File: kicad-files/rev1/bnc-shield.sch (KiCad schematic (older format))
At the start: 113 parts

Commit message: improve robustness and leakage for bnc shield
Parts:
- removed C? (x15): 100nF, symbol C
- removed P? (x7): BNC, symbol BNC
- removed R? (x8): 100k, symbol R
- removed R? (x7): 1.5k, symbol R
- removed R? (x7): 10k, symbol R
- removed U? (x16): SN74LVC1G3157, symbol SN74LVC1G3157
- added C? (x15): 100nF, symbol C
- added P? (x7): BNC, symbol BNC
- added R? (x8): 1M, symbol R
- added R? (x7): 1.5k, symbol R
- added R? (x7): 10k, symbol R
- added U? (x16): TS5A4624, symbol TS5A4624
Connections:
- net labels removed: +5V
- wire segments 432 -> 440
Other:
- moved on the sheet: C?, R?

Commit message: fixed 2.5V regulator resistors
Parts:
- R?: value 124k -> 43.2k
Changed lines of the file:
@@
-EESchema Schematic File Version 2  date Mon 27 May 2013 04:02:44 AM UTC
+EESchema Schematic File Version 2  date Mon 27 May 2013 01:39:56 PM UTC
 LIBS:power
 LIBS:device
@@
 P 6150 8950
 F 0 "R?" V 6230 8950 50  0000 C CNN
-F 1 "124k" V 6150 8950 50  0000 C CNN
+F 1 "43.2k" V 6150 8950 50  0000 C CNN
 F 2 "SM0603" H 6150 8950 60  0001 C CNN
 	1    6150 8950

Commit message: add RS-485 and headers to bnc-shield
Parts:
- removed L?: INDUCTOR, symbol INDUCTOR
- removed P?: CONN_4X2, symbol CONN_4X2
- added C? (x4): 100nF, symbol C
- added C?: 10uF, symbol C
- added D? (x4): DOUBLE_SCHOTTKY, symbol DOUBLE_SCHOTTKY
- added J? (x2): RJ45, symbol RJ45
- added L? (x2): INDUCTOR, symbol INDUCTOR
- added P?: CONN_8X2, symbol CONN_8X2
- added P?: CONN_4, symbol CONN_4
- added P?: ARDUINO_SHIELD, symbol ARDUINO_SHIELD
- added R? (x6): 1k, symbol R
- added R? (x3): 100k, symbol R
- added R?: 120, symbol R
- added R? (x2): 680, symbol R
- added U?: RS485, symbol RS485
- added U? (x2): TS5A4624, symbol TS5A4624
- added U?: 74HC00, symbol 7400
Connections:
- net labels added: +5V, 5V_IN, ADS129x_GPIO1, ADS129x_GPIO2, ADS129x_GPIO3, ADS129x_GPIO4, DAISY_DETECT_NEXT, DAISY_DETECT_NEXT_FILT, DAISY_DETECT_PREVIOUS, DAISY_DETECT_PREVIOUS_FILT, DAISY_ENUMERATION_IN, DAISY_ENUMERATION_IN_FILT, DAISY_ENUMERATION_OUT, DAISY_ENUMERATION_OUT_FILT, GND, PA16, PA17, PA18, PA22, PA23, PA24, PA25, PA26, PA27, PA28, PA29, PA4, PA6, PA8, PA9, PB25, PB27, PC21, PC22, PC23, PC24, PC25, PC26, PC28, PC29, PD7, PD8, RESET, RS485_A, RS485_B, RTS2_RS485_DE, RXD2_RS485_R, TXD2_RS485_D, V_IN
- wire segments 440 -> 606
- no-connect marks 16 -> 19
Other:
- note added: "Biasing and termination for RS-485"
- note added: "DAISY CHAIN NEXT"
- note added: "DAISY CHAIN PREVIOUS"
- note added: "TODO: Replace with SN74LVC1G00DCKR"
- note added: "TODO: according to the SN65HVD78D datasheet, \n we may not need the biasing resistors \n (allowing us to eleminate a switch). \n We should discuss this."
- note added: "e.g. SN65HVD78D"

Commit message: improve text label names
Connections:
- net labels added: PA16_A0, PA17_SDA1, PA18_SCL1, PA22_A3, PA23_A2, PA24_A1, PA25_MISO, PA26_MOSI, PA27_SCLK, PA28_SS0, PA29_SS1, PA4_A5, PA6_A4, PA8_RX, PA9_TX, PB25_PWM2, PB27_PWM13, PC21_PWM9, PC22_PWM8, PC23_PWM7, PC24_PWM6, PC25_PWM5, PC26_PWM4, PC28_PWM3, PC29_PWM10, PD7_PWM11, PD8_PWM12
- net labels removed: PA16, PA17, PA18, PA22, PA23, PA24, PA25, PA26, PA27, PA28, PA29, PA4, PA6, PA8, PA9, PB25, PB27, PC21, PC22, PC23, PC24, PC25, PC26, PC28, PC29, PD7, PD8
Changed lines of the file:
@@
 RESET
 Text Label 26000 5300 0    60   ~ 0
-PA27
+PA27_SCLK
 Text Label 26000 5200 0    60   ~ 0
-PA25
+PA25_MISO
 Text Label 29000 5300 2    60   ~ 0
-PA26
+PA26_MOSI
 $Comp
 L GND #PWR?
@@
 NoConn ~ 29600 3050
 Text Label 29600 2850 2    60   ~ 0
-PA18
+PA18_SCL1
 Text Label 29600 2950 2    60   ~ 0
-PA17
+PA17_SDA1
 $Comp
 L GND #PWR?
@@
 $EndComp
 Text Label 29600 3250 2    60   ~ 0
-PB27
+PB27_PWM13
 Text Label 29600 3350 2    60   ~ 0
-PD8
+PD8_PWM12
 Text Label 29600 3450 2    60   ~ 0
-PD7
+PD7_PWM11
 Text Label 30100 3450 2    60   ~ 0
-PC29
+PC29_PWM10
 Text Label 30100 3550 2    60   ~ 0
-PA28
+PA28_SS0
 Text Label 29600 3650 2    60   ~ 0
-PC21
+PC21_PWM9
 Text Label 29600 3750 2    60   ~ 0
-PC22
+PC22_PWM8
 Text Label 29600 3950 2    60   ~ 0
-PC23
+PC23_PWM7
 Text Label 29600 4050 2    60   ~ 0
-PC24
+PC24_PWM6
 Text Label 29600 4150 2    60   ~ 0
-PC25
+PC25_PWM5
 Text Label 30100 4150 2    60   ~ 0
-PC26
+PC26_PWM4
 Text Label 30100 4250 2    60   ~ 0
-PA29
+PA29_SS1
 Text Label 29600 4350 2    60   ~ 0
-PC28
+PC28_PWM3
 Text Label 29600 4450 2    60   ~ 0
-PB25
+PB25_PWM2
 Text Label 29600 4550 2    60   ~ 0
-PA9
+PA9_TX
 Text Label 29600 4650 2    60   ~ 0
-PA8
+PA8_RX
 Text Label 25500 4650 0    60   ~ 0
-PA4
+PA4_A5
 Text Label 25500 4550 0    60   ~ 0
-PA6
+PA6_A4
 Text Label 25500 4450 0    60   ~ 0
-PA22
+PA22_A3
 Text Label 25500 4350 0    60   ~ 0
-PA23
+PA23_A2
 Text Label 25500 4250 0    60   ~ 0
-PA24
+PA24_A1
 Text Label 25500 4150 0    60   ~ 0
-PA16
+PA16_A0
 $Comp
 L GND #PWR?

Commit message: tidy up the labels and wires on the shields
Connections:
- wire segments 606 -> 744

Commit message: added isolation to BNC shield
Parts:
- removed C? (x2): 10uF, symbol C
- removed C? (x2): 100nF, symbol C
- removed R? (x2): 100k, symbol R
- added C? (x4): 10uF, symbol C
- added C? (x4): 100nF, symbol C
- added L? (x4): MH2029-221Y, symbol INDUCTOR
- added R? (x2): 100k, symbol R
- added U?: SI8661, symbol SI8661
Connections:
- net labels added: LED_LATCH_CLK_ISO, LED_OUTPUT_ENABLE_INPUT_ISO, LED_SERIAL_DAISY_2, LED_SERIAL_DAISY_2_ISO, LED_SERIAL_DAISY_4, LED_SERIAL_DAISY_4_ISO, LED_SHIFT_REG_CLEAR_ISO, LED_SHIFT_REG_CLK_ISO
- wire segments 744 -> 657
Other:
- note added: "Isolated"
- note added: "Not isolated"
- moved on the sheet: C?, D?, L?, P?, R?, U?

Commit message: remove RS-485
 The purpose of the RS-485 was to allow us to synch multiple
devices. However, a better way to do this is to inject a counter
into the samples using the USB Start Of Frame which will be
shared by all devices on the same USB bus.
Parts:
- removed C? (x4): 100nF, symbol C
- removed C?: 10uF, symbol C
- removed D? (x4): DOUBLE_SCHOTTKY, symbol DOUBLE_SCHOTTKY
- removed J? (x2): RJ45, symbol RJ45
- removed L?: INDUCTOR, symbol INDUCTOR
- removed P?: CONN_8X2, symbol CONN_8X2
- removed R? (x6): 1k, symbol R
- removed R? (x3): 100k, symbol R
- removed R?: 120, symbol R
- removed R? (x2): 680, symbol R
- removed U?: RS485, symbol RS485
- removed U? (x2): TS5A4624, symbol TS5A4624
- removed U?: 74HC00, symbol 7400
- added P12: CONN_4X2, symbol CONN_4X2
- gave numbers to parts that had none: 123
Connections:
- net labels removed: 5V_IN, DAISY_DETECT_NEXT, DAISY_DETECT_NEXT_FILT, DAISY_DETECT_PREVIOUS, DAISY_DETECT_PREVIOUS_FILT, DAISY_ENUMERATION_IN, DAISY_ENUMERATION_IN_FILT, DAISY_ENUMERATION_OUT, DAISY_ENUMERATION_OUT_FILT, RS485_A, RS485_B, RTS2_RS485_DE, RXD2_RS485_R, TXD2_RS485_D
- wire segments 657 -> 537
- no-connect marks 19 -> 17
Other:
- note removed: "Biasing and termination for RS-485"
- note removed: "DAISY CHAIN NEXT"
- note removed: "DAISY CHAIN PREVIOUS"
- note removed: "TODO: Replace with SN74LVC1G00DCKR"
- note removed: "TODO: according to the SN65HVD78D datasheet, \n we may not need the biasing resistors \n (allowing us to eleminate a switch). \n We should discuss this."
- note removed: "e.g. SN65HVD78D"

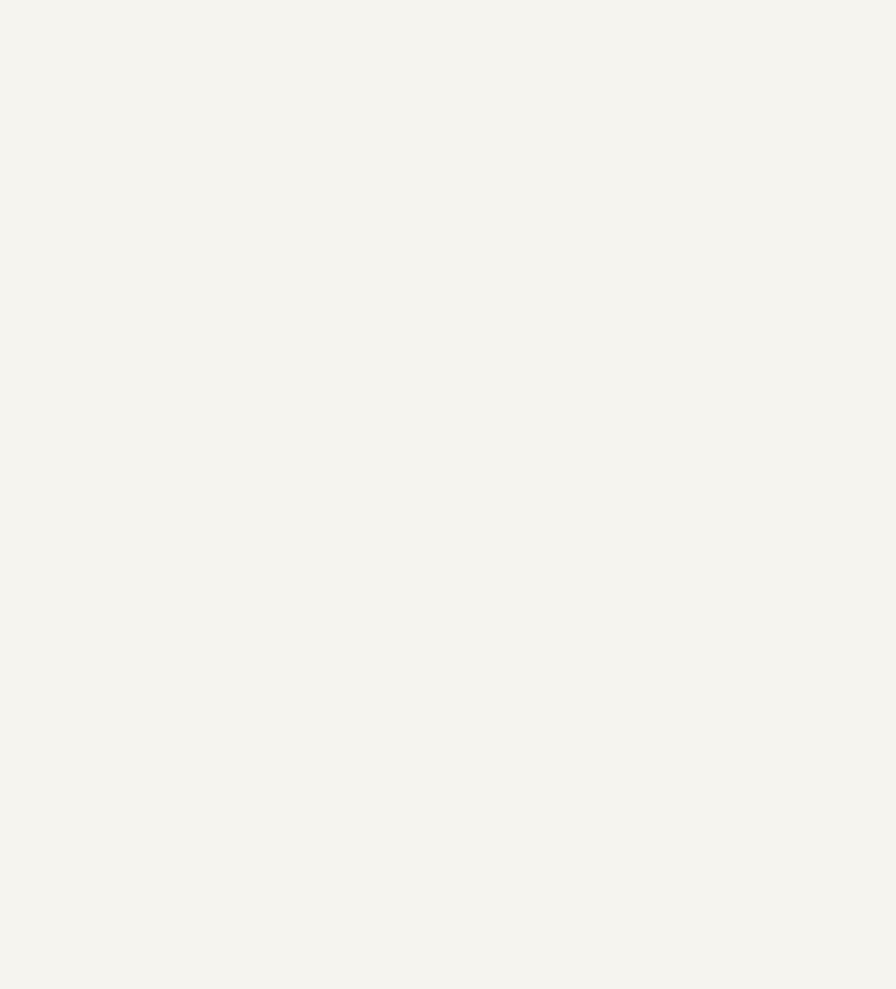
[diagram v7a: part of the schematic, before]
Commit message: added I2C EEPROM to shields
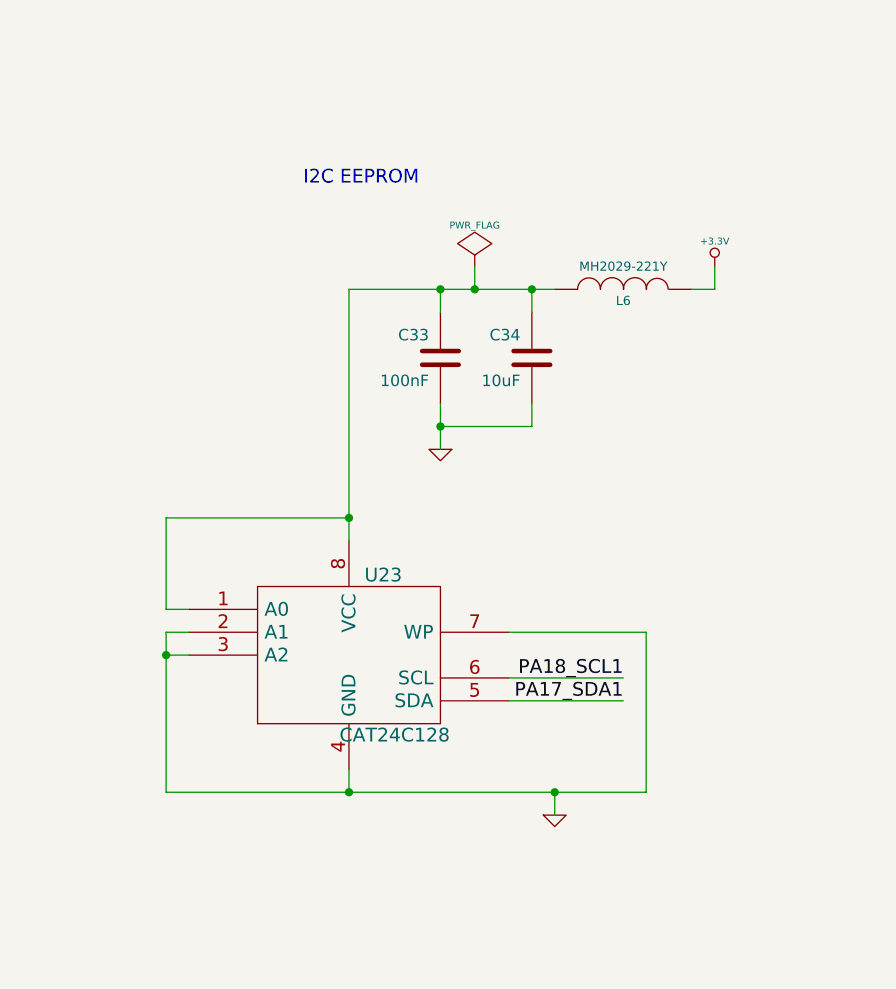
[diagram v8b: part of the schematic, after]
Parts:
- added C33: 100nF, symbol C
- added C34: 10uF, symbol C
- added L6: MH2029-221Y, symbol INDUCTOR
- added U23: CAT24C128, symbol 24C16
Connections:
- wire segments 537 -> 560
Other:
- note added: "I2C EEPROM"
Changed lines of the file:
@@
-EESchema Schematic File Version 2  date Sat 22 Jun 2013 01:22:06 PM CEST
+EESchema Schematic File Version 2  date Sat 22 Jun 2013 02:00:34 PM CEST
 LIBS:power
 LIBS:device
@@
 Comment4 ""
 $EndDescr
+Text Notes 18000 11500 0    60   ~ 0
+I2C EEPROM
+Text Label 19400 13750 2    60   ~ 0
+PA17_SDA1
+Text Label 19400 13650 2    60   ~ 0
+PA18_SCL1
+$Comp
+L GND #PWR79
+U 1 1 51C590FD
+P 19100 14250
+F 0 "#PWR79" H 19100 14250 30  0001 C CNN
+F 1 "GND" H 19100 14180 30  0001 C CNN
+	1    19100 14250
+	1    0    0    -1
+$EndComp
+$Comp
+L GND #PWR76
+U 1 1 51C590FC
+P 18600 12650
+F 0 "#PWR76" H 18600 12650 30  0001 C CNN
+F 1 "GND" H 18600 12580 30  0001 C CNN
+	1    18600 12650
+	-1   0    0    -1
+$EndComp
+$Comp
+L +3.3V #PWR80
+U 1 1 51C590FB
+P 19800 11850
+F 0 "#PWR80" H 19800 11810 30  0001 C CNN
+F 1 "+3.3V" H 19800 11960 30  0000 C CNN
+	1    19800 11850
+	-1   0    0    -1
+$EndComp
+$Comp
+L C C33
+U 1 1 51C590FA
+P 18600 12250
+F 0 "C33" H 18650 12350 50  0000 L CNN
+F 1 "100nF" H 18650 12150 50  0000 L CNN
+	1    18600 12250
+	-1   0    0    -1
+$EndComp
+$Comp
+L INDUCTOR L6
+U 1 1 51C590F9
+P 19400 11950
+F 0 "L6" V 19350 11950 40  0000 C CNN
+F 1 "MH2029-221Y" V 19500 11950 40  0000 C CNN
+	1    19400 11950
+	0    1    -1   0
+$EndComp
+$Comp
+L C C34
+U 1 1 51C590F8
+P 19000 12250
+F 0 "C34" H 19050 12350 50  0000 L CNN
+F 1 "10uF" H 19050 12150 50  0000 L CNN
+	1    19000 12250
+	-1   0    0    -1
+$EndComp
+$Comp
+L PWR_FLAG #FLG8
+U 1 1 51C590F7
+P 18750 11850
+F 0 "#FLG8" H 18750 11945 30  0001 C CNN
+F 1 "PWR_FLAG" H 18750 12030 30  0000 C CNN
+	1    18750 11850
+	-1   0    0    -1
+$EndComp
+$Comp
+L 24C16 U23
+U 1 1 51C590F6
+P 18200 13550
+F 0 "U23" H 18350 13900 60  0000 C CNN
+F 1 "CAT24C128" H 18400 13200 60  0000 C CNN
+	1    18200 13550
+	1    0    0    -1
+$EndComp
+Wire Wire Line
+	18200 11950 18200 13050
+Wire Wire Line
+	18200 14050 18200 14150
+Wire Wire Line
+	19400 13650 18900 13650
+Connection ~ 17400 13550
+Wire Wire Line
+	17500 13550 17400 13550
+Connection ~ 18200 14150
+Wire Wire Line
+	17400 13350 17500 13350
+Wire Wire Line
+	19800 11950 19800 11850
+Wire Wire Line
+	19700 11950 19800 11950
+Connection ~ 18600 12550
+Wire Wire Line
+	19000 12550 19000 12450
+Wire Wire Line
+	18600 12550 19000 12550
+Connection ~ 18750 11950
+Wire Wire Line
+	18750 11950 18750 11850
+Connection ~ 19000 11950
+Wire Wire Line
+	19000 11950 19000 12050
+Wire Wire Line
+	18600 12050 18600 11950
+Connection ~ 18600 11950
+Wire Wire Line
+	18600 12650 18600 12450
+Wire Wire Line
+	19100 11950 18200 11950
+Wire Wire Line
+	17400 13450 17500 13450
+Wire Wire Line
+	18900 13750 19400 13750
+Wire Wire Line
+	19500 13450 18900 13450
+Wire Wire Line
+	19500 14150 19500 13450
+Wire Wire Line
+	17400 14150 19500 14150
+Wire Wire Line
+	19100 14250 19100 14150
+Connection ~ 19100 14150
+Wire Wire Line
+	17400 14150 17400 13450
+Wire Wire Line
+	17400 12950 17400 13350
+Wire Wire Line
+	18200 12950 17400 12950
+Connection ~ 18200 12950
 Connection ~ 20100 5050
 Wire Wire Line
@@
 PA26_MOSI
 $Comp
-L GND #PWR80
+L GND #PWR83
 U 1 1 51B42FE6
 P 20800 3850
-F 0 "#PWR80" H 20800 3850 30  0001 C CNN
+F 0 "#PWR83" H 20800 3850 30  0001 C CNN
 F 1 "GND" H 20800 3780 30  0001 C CNN
 	1    20800 3850
@@
 $EndComp
 $Comp
-L +5V #PWR79
+L +5V #PWR82
 U 1 1 51B42FE5
 P 20800 3350
-F 0 "#PWR79" H 20800 3440 20  0001 C CNN
+F 0 "#PWR82" H 20800 3440 20  0001 C CNN
 F 1 "+5V" H 20800 3440 30  0000 C CNN
 	1    20800 3350
@@
 PA17_SDA1
 $Comp
-L GND #PWR82
+L GND #PWR85
 U 1 1 51B42FE4
 P 22300 1550
-F 0 "#PWR82" H 22300 1550 30  0001 C CNN
+F 0 "#PWR85" H 22300 1550 30  0001 C CNN
 F 1 "GND" H 22300 1480 30  0001 C CNN
 	1    22300 1550
@@
 LED_LATCH_CLK
 $Comp
-L GND #PWR78
+L GND #PWR81
 U 1 1 51B42CF4
 P 20100 5100
-F 0 "#PWR78" H 20100 5100 30  0001 C CNN
+F 0 "#PWR81" H 20100 5100 30  0001 C CNN
 F 1 "GND" H 20100 5030 30  0001 C CNN
 	1    20100 5100
@@
 LED_SERIAL
 $Comp
-L PWR_FLAG #FLG8
+L PWR_FLAG #FLG9
 U 1 1 51B42CF3
 P 20300 5000
-F 0 "#FLG8" H 20300 5095 30  0001 C CNN
+F 0 "#FLG9" H 20300 5095 30  0001 C CNN
 F 1 "PWR_FLAG" H 20300 5180 30  0000 C CNN
 	1    20300 5000
@@
 $EndComp
 $Comp
-L +3.3V #PWR81
+L +3.3V #PWR84
 U 1 1 51A2902C
 P 20950 8600
-F 0 "#PWR81" H 20950 8560 30  0001 C CNN
+F 0 "#PWR84" H 20950 8560 30  0001 C CNN
 F 1 "+3.3V" H 20950 8710 30  0000 C CNN
 	1    20950 8600
@@
 $EndComp
 $Comp
-L DGND #PWR83
+L DGND #PWR86
 U 1 1 51A2902B
 P 22600 8950
-F 0 "#PWR83" H 22600 8950 40  0001 C CNN
+F 0 "#PWR86" H 22600 8950 40  0001 C CNN
 F 1 "DGND" H 22600 8880 40  0000 C CNN
 	1    22600 8950
@@
 $EndComp
 $Comp
-L DGND #PWR76
+L DGND #PWR77
 U 1 1 51A29028
 P 18750 6800
-F 0 "#PWR76" H 18750 6800 40  0001 C CNN
+F 0 "#PWR77" H 18750 6800 40  0001 C CNN
 F 1 "DGND" H 18750 6730 40  0000 C CNN
 	1    18750 6800
@@
 $EndComp
 $Comp
-L DGND #PWR77
+L DGND #PWR78
 U 1 1 51A29027
 P 18750 9200
-F 0 "#PWR77" H 18750 9200 40  0001 C CNN
+F 0 "#PWR78" H 18750 9200 40  0001 C CNN
 F 1 "DGND" H 18750 9130 40  0000 C CNN
 	1    18750 9200
